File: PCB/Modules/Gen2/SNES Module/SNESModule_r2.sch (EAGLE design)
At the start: 17 parts, among them IC1 SN65HVD31DR, IC2 LM3480-5.0

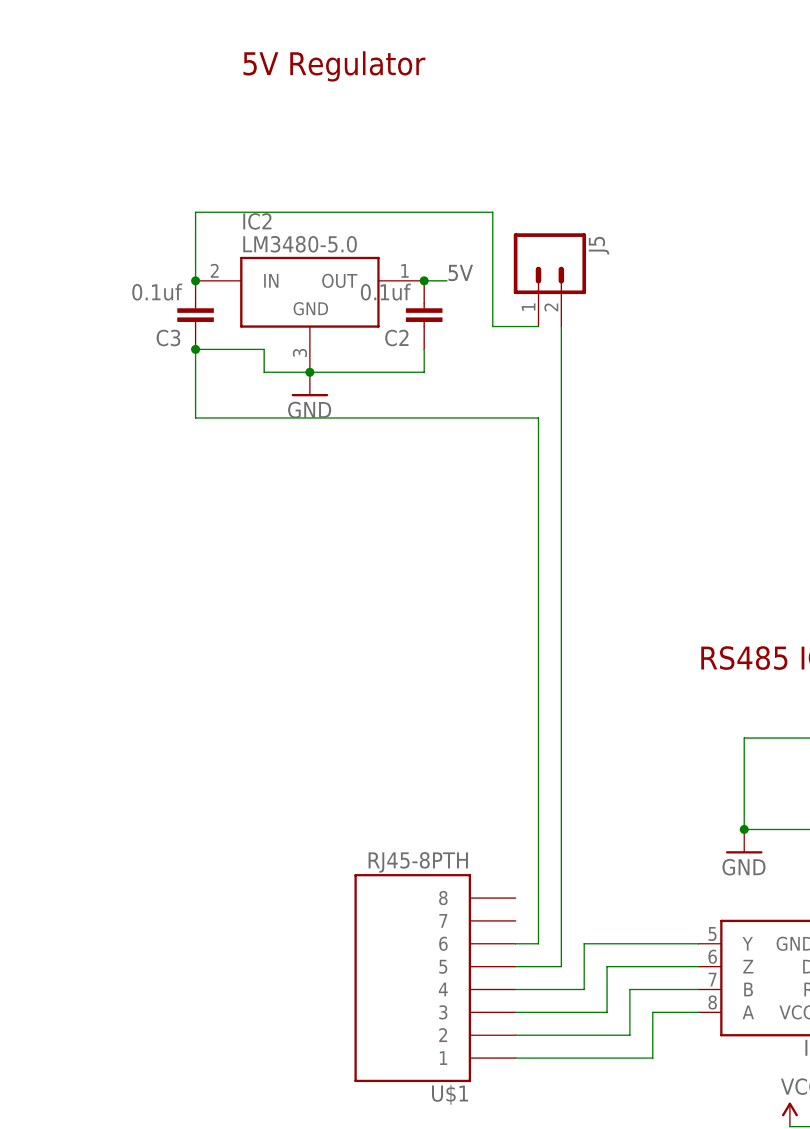
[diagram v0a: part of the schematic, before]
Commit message: -Critical Update for modules with optional RJ45 power (ValveDriver, I2C, SNES and DDS); new PCB designs add a diode to prevent USB power from entering output pin of 5V regulator, when RJ45 (state machine) power is not connected. This update greatly reduces unnecessary power consumption and heat dissipation. If you built a board using the previous designs, please Email a photo of your board to Sanworks support for a free upgrade. -Updated component names on some boards and on web BOMs to avoid skipping parts -Renamed Gen2 module PCB folder from '0.7' to 'Gen2' -Retired pocket state machine (to be replaced with Bpod State Machine r1)
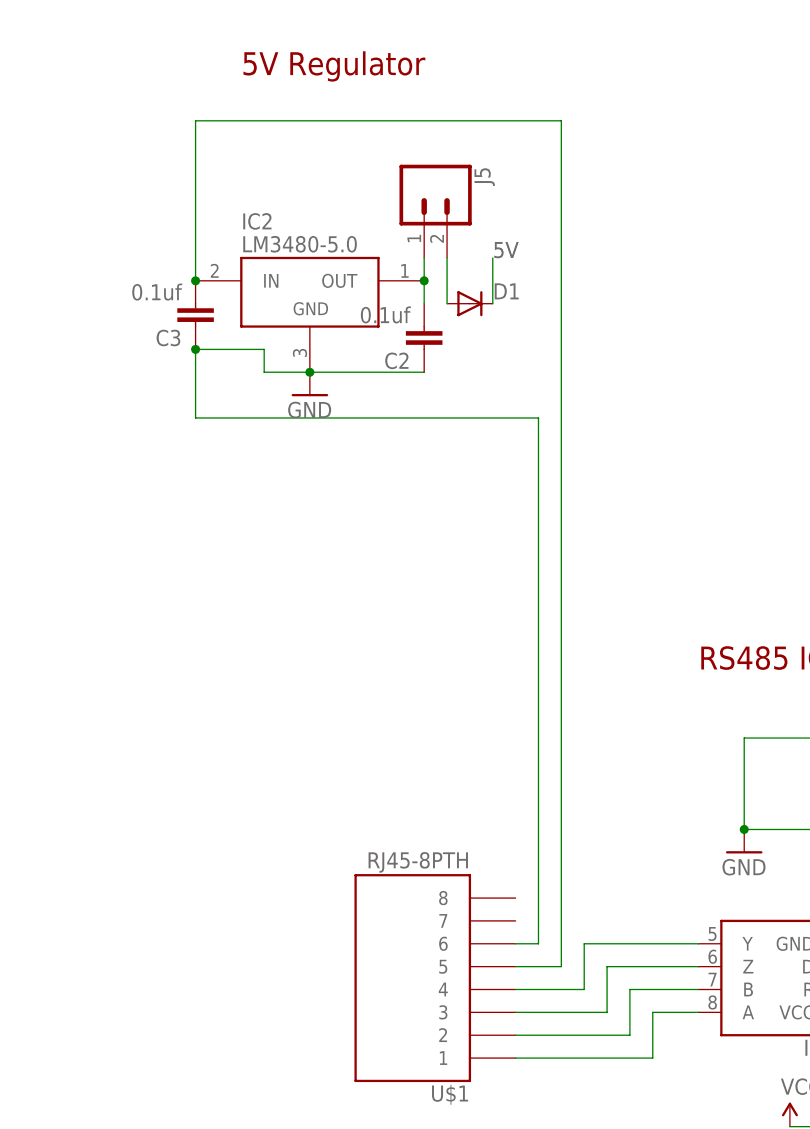
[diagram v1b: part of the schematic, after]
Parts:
- added D1: MBR0520LT, diode:MBR0520LT
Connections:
- removed net N$24: J5.2, U$1.5
- new net N$11: D1.A, J5.2
- new net N$5: C2.2, IC2.OUT, J5.1
- net 5V: now also D1.C; no longer C2.2, IC2.OUT
- net N$26: now also U$1.5; no longer J5.1
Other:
- moved on the sheet: C2, J5
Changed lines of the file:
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@@
 <part name="J1" library="SparkFun-Connectors" deviceset="M04" device="PTH"/>
 <part name="FRAME1" library="frames" deviceset="A4L-LOC" device=""/>
+<part name="D1" library="diode" deviceset="MBR0520LT" device=""/>
 </parts>
 <sheets>
@@
 <plain>
 <text x="124.46" y="68.58" size="1.778" layer="97">5V</text>
-<text x="60.96" y="119.38" size="1.778" layer="97">5V</text>
+<text x="66.04" y="121.92" size="1.778" layer="97">5V</text>
 <text x="3.048" y="6.604" size="2.54" layer="94" font="vector">Please read GPL v3.0 for license terms. http//www.gnu.org/licenses/gpl-3.0.en.html</text>
 <text x="1.778" y="11.43" size="2.54" layer="94" font="vector">NOTE: This design file is part of the Sanworks Bpod-CAD repository. (C) 2017 Sanworks LLC</text>
@@
 <instance part="H3" gate="G$1" x="190.5" y="53.34"/>
 <instance part="H4" gate="G$1" x="190.5" y="60.96"/>
-<instance part="J5" gate="G$1" x="71.12" y="121.92" rot="R270"/>
+<instance part="J5" gate="G$1" x="58.42" y="129.54" rot="R270"/>
 <instance part="IC2" gate="G$1" x="45.72" y="119.38"/>
-<instance part="C2" gate="G$1" x="58.42" y="116.84" rot="R180"/>
+<instance part="C2" gate="G$1" x="58.42" y="114.3" rot="R180"/>
 <instance part="C3" gate="G$1" x="33.02" y="116.84" rot="R180"/>
 <instance part="GND5" gate="1" x="45.72" y="106.68"/>
@@
 <instance part="J1" gate="G$1" x="193.04" y="73.66" rot="MR90"/>
 <instance part="FRAME1" gate="G$1" x="-7.62" y="-20.32"/>
+<instance part="D1" gate="G$1" x="63.5" y="116.84" smashed="yes">
+<attribute name="NAME" x="66.04" y="117.3226" size="1.778" layer="95"/>
+</instance>
 </instances>
 <busses>
@@
 <pinref part="C2" gate="G$1" pin="1"/>
 <wire x1="45.72" y1="109.22" x2="58.42" y2="109.22" width="0.1524" layer="91"/>
-<wire x1="58.42" y1="109.22" x2="58.42" y2="111.76" width="0.1524" layer="91"/>
 <junction x="45.72" y="109.22"/>
 <pinref part="GND5" gate="1" pin="GND"/>
@@
 </segment>
 <segment>
-<pinref part="IC2" gate="G$1" pin="OUT"/>
-<wire x1="58.42" y1="119.38" x2="60.96" y2="119.38" width="0.1524" layer="91"/>
-<pinref part="C2" gate="G$1" pin="2"/>
-<junction x="58.42" y="119.38"/>
-</segment>
-</net>
-<net name="N$24" class="0">
-<segment>
-<pinref part="U$1" gate="G$1" pin="5"/>
-<pinref part="J5" gate="G$1" pin="2"/>
-<wire x1="68.58" y1="43.18" x2="73.66" y2="43.18" width="0.1524" layer="91"/>
-<wire x1="73.66" y1="43.18" x2="73.66" y2="114.3" width="0.1524" layer="91"/>
+<pinref part="D1" gate="G$1" pin="C"/>
+<wire x1="66.04" y1="116.84" x2="66.04" y2="121.92" width="0.1524" layer="91"/>
 </segment>
 </net>
 <net name="N$26" class="0">
 <segment>
-<pinref part="J5" gate="G$1" pin="1"/>
-<wire x1="71.12" y1="114.3" x2="66.04" y2="114.3" width="0.1524" layer="91"/>
-<wire x1="66.04" y1="114.3" x2="66.04" y2="127" width="0.1524" layer="91"/>
 <pinref part="IC2" gate="G$1" pin="IN"/>
-<wire x1="66.04" y1="127" x2="33.02" y2="127" width="0.1524" layer="91"/>
-<wire x1="33.02" y1="127" x2="33.02" y2="119.38" width="0.1524" layer="91"/>
+<wire x1="73.66" y1="137.16" x2="33.02" y2="137.16" width="0.1524" layer="91"/>
+<wire x1="33.02" y1="137.16" x2="33.02" y2="119.38" width="0.1524" layer="91"/>
 <pinref part="C3" gate="G$1" pin="2"/>
 <junction x="33.02" y="119.38"/>
+<pinref part="U$1" gate="G$1" pin="5"/>
+<wire x1="68.58" y1="43.18" x2="73.66" y2="43.18" width="0.1524" layer="91"/>
+<wire x1="73.66" y1="137.16" x2="73.66" y2="43.18" width="0.1524" layer="91"/>
 </segment>
 </net>
@@
 </segment>
 </net>
+<net name="N$5" class="0">
+<segment>
+<pinref part="IC2" gate="G$1" pin="OUT"/>
+<pinref part="J5" gate="G$1" pin="1"/>
+<wire x1="58.42" y1="119.38" x2="58.42" y2="121.92" width="0.1524" layer="91"/>
+<pinref part="C2" gate="G$1" pin="2"/>
+<wire x1="58.42" y1="116.84" x2="58.42" y2="119.38" width="0.1524" layer="91"/>
+<junction x="58.42" y="119.38"/>
+</segment>
+</net>
+<net name="N$11" class="0">
+<segment>
+<pinref part="J5" gate="G$1" pin="2"/>
+<pinref part="D1" gate="G$1" pin="A"/>
+<wire x1="60.96" y1="116.84" x2="60.96" y2="121.92" width="0.1524" layer="91"/>
+</segment>
+</net>
